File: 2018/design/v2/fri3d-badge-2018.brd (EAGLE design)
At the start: 80 x 60 mm, 136 parts

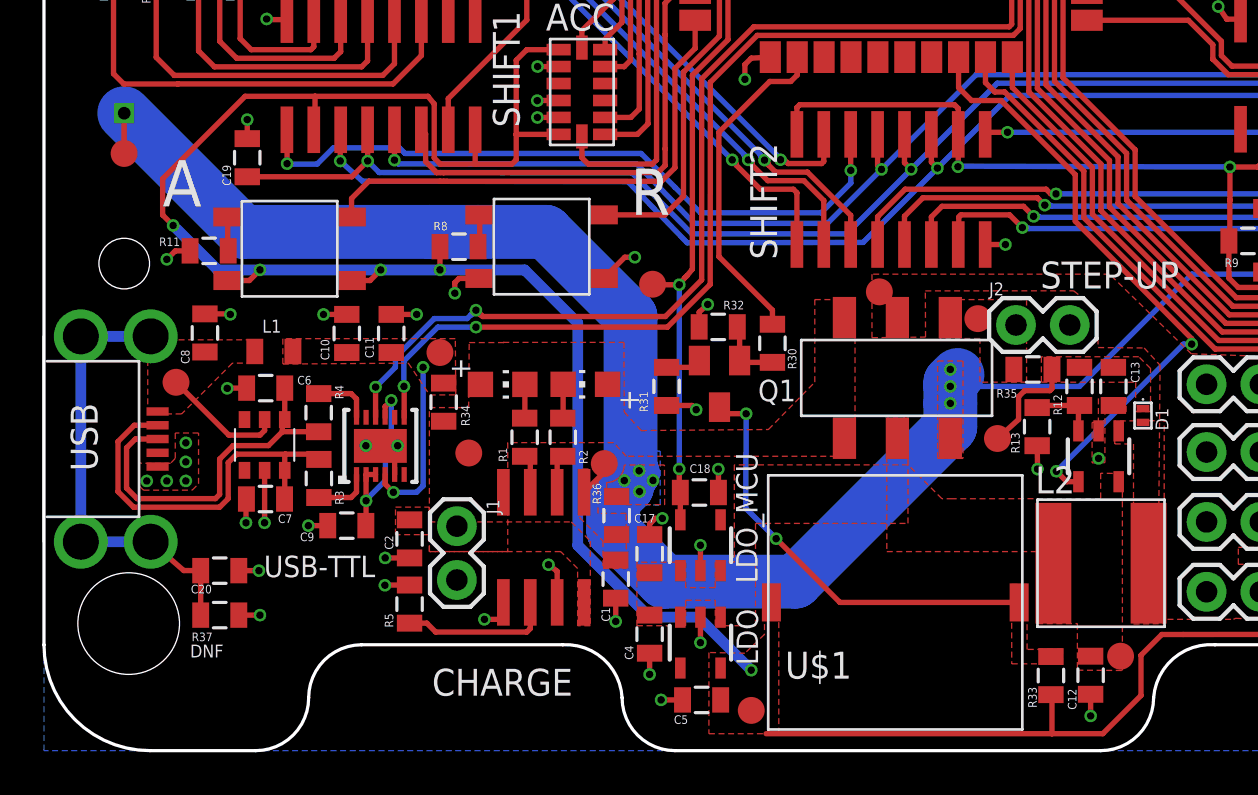
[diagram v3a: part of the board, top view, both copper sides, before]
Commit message: fixed incorrect footprint for sx1308
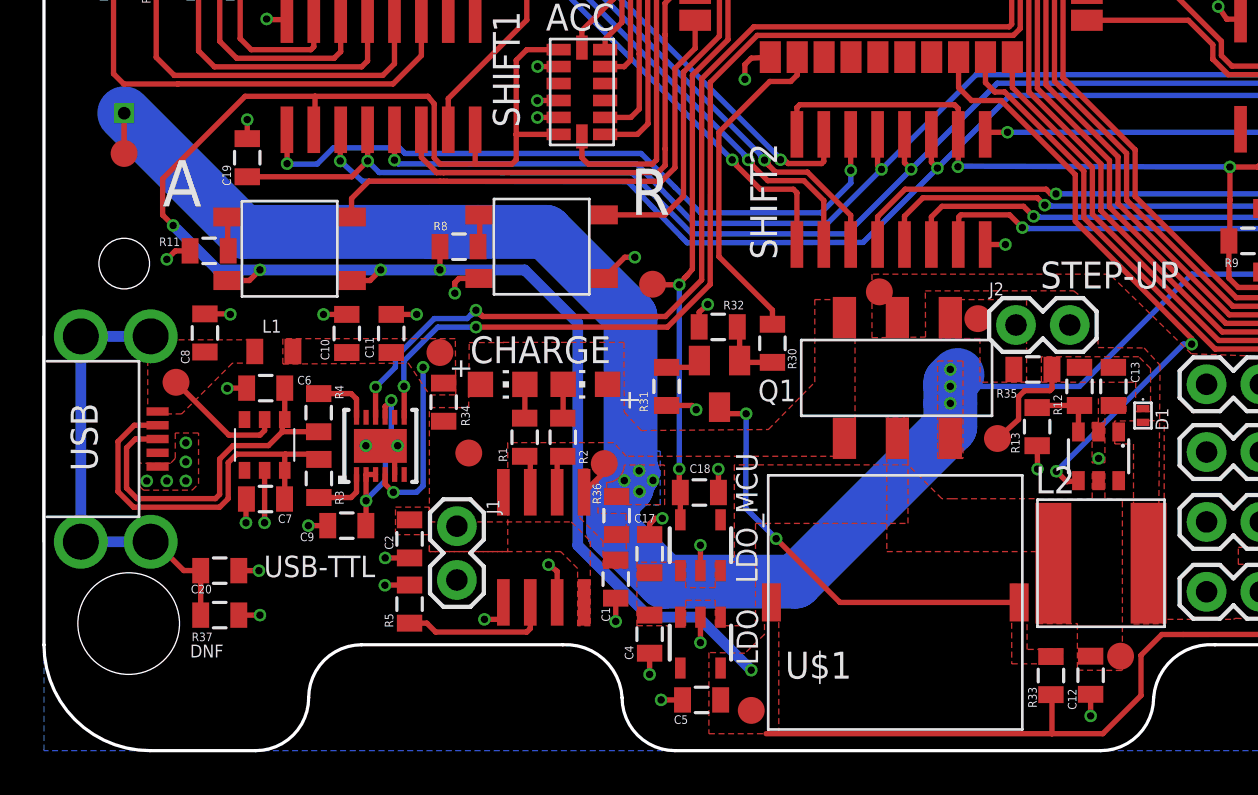
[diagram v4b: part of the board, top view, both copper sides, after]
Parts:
- STEP-UP: device power:SOT23-5 -> power:SOT23-6
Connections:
- net D+: now also USB.D+; no longer USB.3
- net D-: now also USB.D-; no longer USB.2
- net GND: now also USB.GND; no longer USB.5
- net N$23: now also USB.P$6, USB.P$7, USB.P$8, USB.P$9; no longer USB.6, USB.7, USB.8, USB.9
- net USB-RAW: now also USB.VBUS; no longer USB.1
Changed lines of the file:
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@@
 <drawing>
 <settings>
-<setting alwaysvectorfont="yes"/>
+<setting alwaysvectorfont="no"/>
 <setting verticaltext="up"/>
 </settings>
@@
 </layers>
 <board>
+<fusionsync huburn="a.cGVyc29uYWw6dWUyYmEzZWJl" projecturn="a.cGVyc29uYWw6dWUyYmEzZWJlIzIwMTcwNTAyNzQzNTk5NzY" f3durn="urn:adsk.wipprod:dm.lineage:U4Jl31eAR-afP-OGFtuy1g" pcbguid="dd80eeac-d1cc-4027-afa2-cc44859ce9eb" lastpulledtime="" lastsyncedchangeguid="81a200b9-d31d-708b-0bff-8fa8a62ca3eb"/>
 <plain>
 <hole x="4" y="54" drill="4.8"/>
@@
 </element>
 <element name="CHARGE" library="power" package="SO8" value="TP4056" x="23.6" y="9.6" smashed="yes">
-<attribute name="NAME" x="18.325" y="2.595" size="1.27" layer="25"/>
+<attribute name="NAME" x="20.125" y="18.295" size="1.27" layer="25"/>
 </element>
 <element name="C1" library="passive" package="0805" value="10uF" x="27" y="8.1" smashed="yes" rot="R270">
@@
 <attribute name="VALUE" x="6.384" y="24.403" size="0.4064" layer="27"/>
 </element>
-<element name="STEP-UP" library="power" package="SOT23-5" value="SX1308" x="49.8" y="13.9" smashed="yes" rot="R180">
+<element name="STEP-UP" library="power" package="SOT23-6" value="SX1308" x="49.8" y="13.9" smashed="yes" rot="R180">
 <attribute name="NAME" x="53.605" y="23.095" size="1.27" layer="25" rot="R180"/>
 </element>
@@
 <signals>
 <signal name="GND">
-<contactref element="USB" pad="5"/>
+<contactref element="USB" pad="GND"/>
 <contactref element="USB-TTL" pad="5"/>
 <contactref element="USB-TTL" pad="13"/>
@@
 </signal>
 <signal name="D+">
-<contactref element="USB" pad="3"/>
+<contactref element="USB" pad="D+"/>
 <contactref element="R4" pad="1"/>
 <contactref element="C6" pad="1"/>
@@
 <contactref element="R3" pad="1"/>
 <contactref element="C7" pad="1"/>
-<contactref element="USB" pad="2"/>
+<contactref element="USB" pad="D-"/>
 <wire x1="5.365" y1="15.365" x2="4.265" y2="15.365" width="0.254" layer="1"/>
 <wire x1="3.496" y1="12.23265625" x2="4.23265625" y2="11.496" width="0.254" layer="1"/>
@@
 </signal>
 <signal name="USB-RAW">
-<contactref element="USB" pad="1"/>
+<contactref element="USB" pad="VBUS"/>
 <contactref element="L1" pad="1"/>
 <contactref element="C8" pad="1"/>
@@
 <vertex x="48.8" y="3.8"/>
 <vertex x="50.925" y="3.785"/>
-<vertex x="50.925" y="13.085"/>
-<vertex x="49.9" y="13.1"/>
-<vertex x="49.9" y="11.9"/>
+<vertex x="50.925" y="11.885"/>
+<vertex x="50.1" y="11.91"/>
+<vertex x="50.1" y="13.1"/>
+<vertex x="49.5" y="13.1"/>
+<vertex x="49.5" y="11.9"/>
 <vertex x="42.91" y="11.895"/>
 <vertex x="42.405" y="11.895"/>
@@
 <wire x1="43.19" y1="31.31" x2="43.19" y2="32.75" width="0.254" layer="1"/>
 <wire x1="54.200825" y1="19.449175" x2="48.7" y2="25" width="0.254" layer="1"/>
-<wire x1="48.85" y1="12.7" x2="48.3" y2="12.7" width="0.254" layer="1"/>
+<wire x1="48.85" y1="12.75" x2="48.3" y2="12.7" width="0.254" layer="1"/>
 <wire x1="48.3" y1="12.7" x2="47.808003125" y2="13.191996875" width="0.254" layer="1"/>
 <via x="47.808003125" y="13.191996875" extent="1-16" drill="0.35"/>
@@
 <contactref element="R13" pad="2"/>
 <contactref element="STEP-UP" pad="3"/>
-<wire x1="48.85" y1="15.1" x2="48.85" y2="16.25" width="0.254" layer="1"/>
+<wire x1="48.85" y1="15.05" x2="48.85" y2="16.25" width="0.254" layer="1"/>
 <wire x1="48.85" y1="16.25" x2="48.9" y2="16.3" width="0.254" layer="1"/>
 <wire x1="48.9" y1="16.3" x2="47" y2="16.3" width="0.254" layer="1"/>
@@
 <contactref element="SHIFT1" pad="14"/>
 <contactref element="MCU" pad="13"/>
-<wire x1="18.421825" y1="27.41683125" x2="18.535621875" y2="27.298984375" width="0.254" layer="1"/>
-<wire x1="18.535621875" y1="27.298984375" x2="18.53974375" y2="27.2989125" width="0.254" layer="1"/>
-<wire x1="18.53974375" y1="27.2989125" x2="18.54265625" y2="27.296" width="0.254" layer="1"/>
+<wire x1="18.54265625" y1="27.296" x2="18.53974375" y2="27.2989125" width="0.254" layer="1"/>
 <wire x1="18.54265625" y1="27.296" x2="18.706334375" y2="27.296" width="0.254" layer="1"/>
 <wire x1="18.706334375" y1="27.296" x2="18.870253125" y2="27.293134375" width="0.254" layer="1"/>
 <wire x1="18.870253125" y1="27.293134375" x2="18.873221875" y2="27.296" width="0.254" layer="1"/>
-<wire x1="17.822" y1="29.32" x2="18.022134375" y2="29.119865625" width="0.254" layer="1"/>
 <wire x1="18.873221875" y1="27.296" x2="28.993021875" y2="27.296" width="0.254" layer="1"/>
 <wire x1="28.993021875" y1="27.296" x2="28.997021875" y2="27.3" width="0.254" layer="1"/>
 <wire x1="28.997021875" y1="27.3" x2="29" y2="27.3" width="0.254" layer="1"/>
-<wire x1="18.022134375" y1="29.119865625" x2="18.022134375" y2="27.816521875" width="0.254" layer="1"/>
-<wire x1="18.022134375" y1="27.816521875" x2="18.421825" y2="27.41683125" width="0.254" layer="1"/>
 <wire x1="29" y1="27.3" x2="29.332" y2="27.632" width="0.254" layer="1"/>
 <wire x1="29.329" y1="33.803440625" x2="29.329" y2="35.3" width="0.254" layer="1"/>
@@
 <wire x1="29.332" y1="28.41615" x2="29.332828125" y2="28.416978125" width="0.254" layer="1"/>
 <wire x1="29.332" y1="27.632" x2="29.332" y2="28.41615" width="0.254" layer="1"/>
+<wire x1="18.53974375" y1="27.2989125" x2="18.535621875" y2="27.298984375" width="0.254" layer="1"/>
+<wire x1="18.535621875" y1="27.298984375" x2="18.421825" y2="27.41683125" width="0.254" layer="1"/>
+<wire x1="18.421825" y1="27.41683125" x2="17.822" y2="28.01665625" width="0.254" layer="1"/>
+<wire x1="17.822" y1="28.01665625" x2="17.822" y2="29.32" width="0.254" layer="1"/>
 </signal>
 <signal name="LEDS_SCK">
@@
 <contactref element="C20" pad="1"/>
 <contactref element="R37" pad="2"/>
-<contactref element="USB" pad="9"/>
-<contactref element="USB" pad="6"/>
-<contactref element="USB" pad="7"/>
-<contactref element="USB" pad="8"/>
-<wire x1="1.74" y1="19.565" x2="5.04" y2="19.565" width="0.508" layer="16"/>
-<wire x1="5.04" y1="9.865" x2="1.74" y2="9.865" width="0.508" layer="16"/>
-<wire x1="1.74" y1="9.865" x2="1.74" y2="19.565" width="0.508" layer="16"/>
+<contactref element="USB" pad="P$9"/>
+<contactref element="USB" pad="P$6"/>
+<contactref element="USB" pad="P$7"/>
+<contactref element="USB" pad="P$8"/>
 <wire x1="7.4" y1="6.4" x2="7.4" y2="8.5" width="0.254" layer="1"/>
 <wire x1="7.4" y1="8.5" x2="6.6" y2="8.505" width="0.254" layer="1"/>
-<wire x1="6.6" y1="8.505" x2="5.04" y2="9.865" width="0.254" layer="1"/>
+<wire x1="5.04" y1="19.565" x2="1.74" y2="19.565" width="0.508" layer="16"/>
+<wire x1="1.74" y1="19.565" x2="1.74" y2="9.865" width="0.508" layer="16"/>
+<wire x1="1.74" y1="9.865" x2="5.04" y2="9.865" width="0.508" layer="16"/>
+<wire x1="6.6" y1="8.505" x2="5.24" y2="9.865" width="0.254" layer="1"/>
+<wire x1="5.24" y1="9.865" x2="5.04" y2="9.865" width="0.254" layer="1"/>
 </signal>
 </signals>
@@
 </note>
 <note version="8.3" severity="warning">
+Since Version 8.3, EAGLE supports Fusion synchronisation.
+This feature will not be available in this version and saving
+the document will break the link to the Fusion PCB feature.
+</note>
+<note version="8.3" severity="warning">
